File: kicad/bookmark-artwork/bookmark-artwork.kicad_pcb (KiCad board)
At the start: 2 copper layers, 44.9 x 150 mm, 6 parts

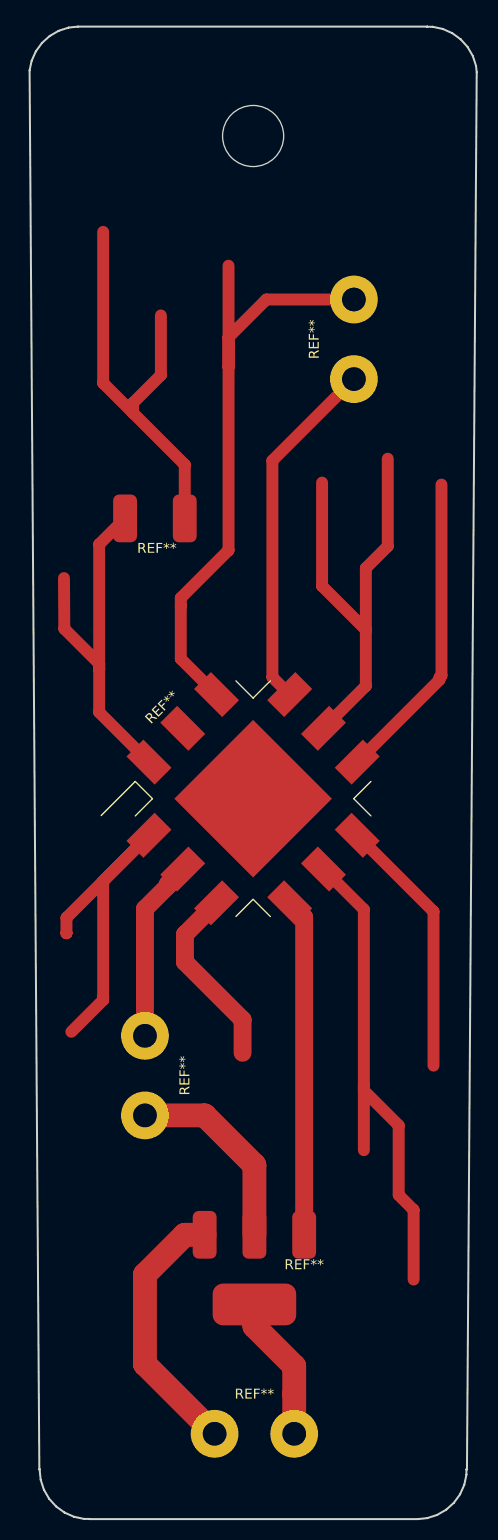
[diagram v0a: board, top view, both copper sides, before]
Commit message: Add fiducial to better center pattern
Also increase edge guard slightly and make tweaks to the
design to better fit.
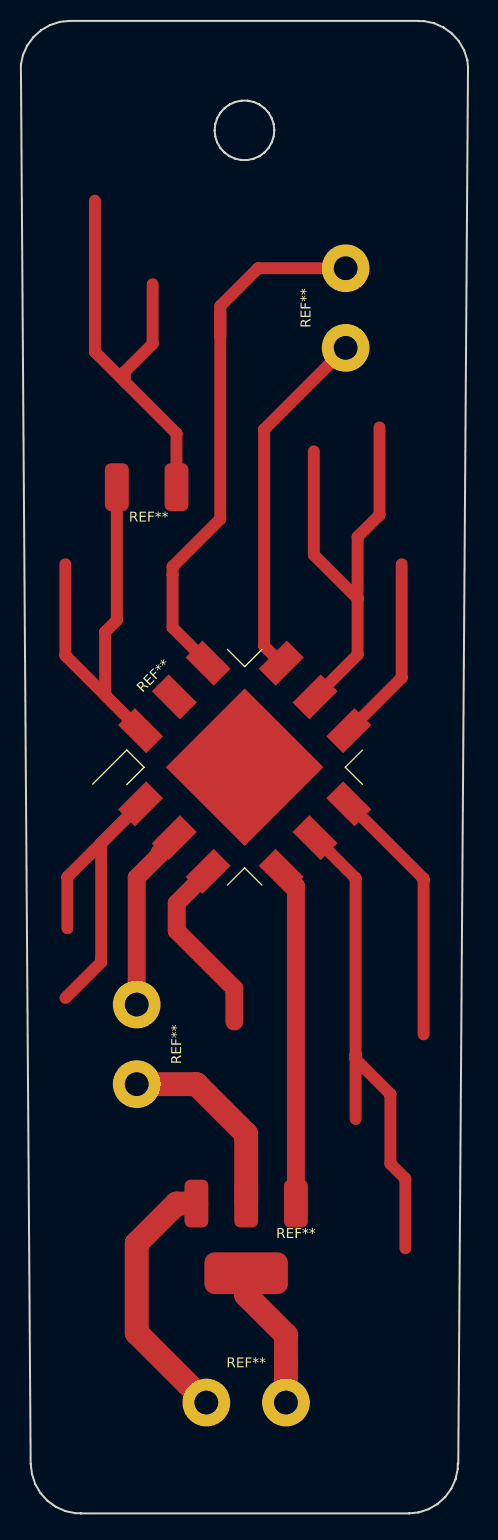
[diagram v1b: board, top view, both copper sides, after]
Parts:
- removed the REF** at (36.0, 155.0)
- removed the REF** at (25.0, 119.0)
- removed the REF** at (46.0, 45.0)
- removed the REF** at (36.0, 137.0)
- removed the REF** at (26.0, 63.0)
- added REF**: p, p, F.Cu at (35.2, 151.9)
- added REF**: p, p, F.Cu at (24.2, 115.9)
- added REF**: p, p, F.Cu at (45.2, 41.9)
- added REF**: p, p, F.Cu at (35.2, 133.9)
- added REF**: p, p, F.Cu at (25.2, 59.9)
- moved REF** 3.27 mm to (35.0, 88.0)
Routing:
- net (no net): track 505.3 -> 495.0 mm
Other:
- outline, holes or cut-outs redrawn

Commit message: Rework circuit artwork to improve printability and spacing
- shrank square "pad" in center by 1.6 mm
- reworked a few traces to account for 5 mm border
  around whole edge rather than 3 mm
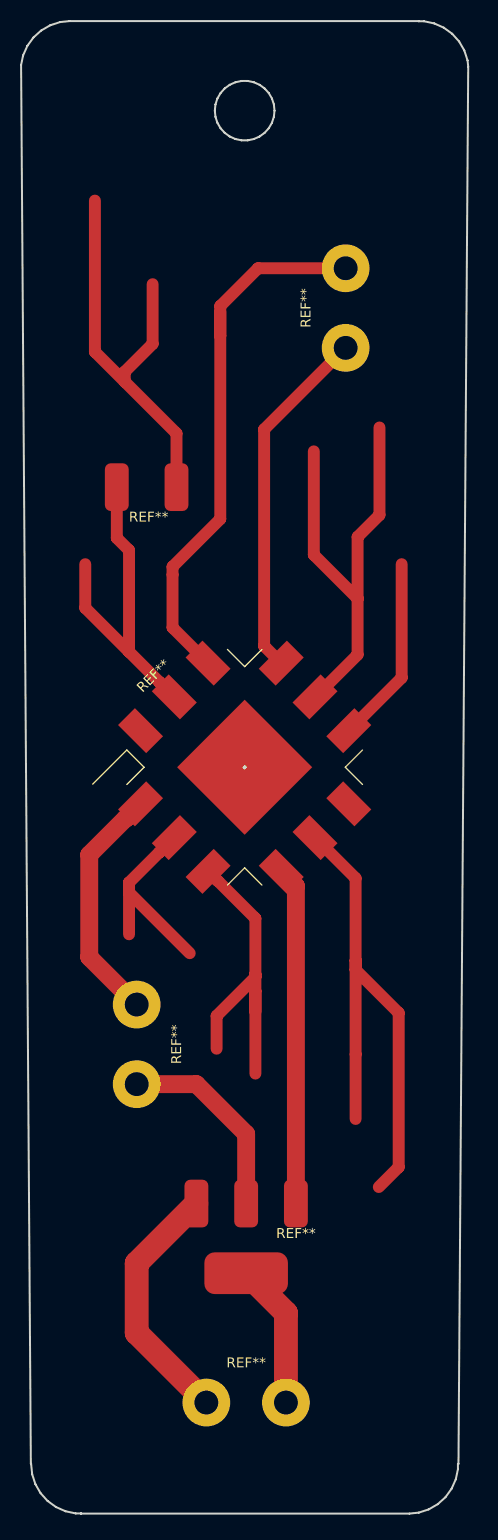
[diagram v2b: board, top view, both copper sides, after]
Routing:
- net (no net): track 495.0 -> 462.9 mm
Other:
- outline, holes or cut-outs redrawn
